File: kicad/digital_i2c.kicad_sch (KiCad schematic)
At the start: 21 parts, among them J10 Qwiic Cell Density, J11 Qwiic EZO-pH, J12 Qwiic EZO-ORP, J13 Qwiic EZO-DO, J14 Qwiic EZO-RTD, J15 Load Cell, J16 RS485 Hamilton, J8 Qwiic GPS SAM-M8Q, J9 Qwiic RTC DS3231, U14 HX711, U15 MAX485ESA, U21 ISO1541

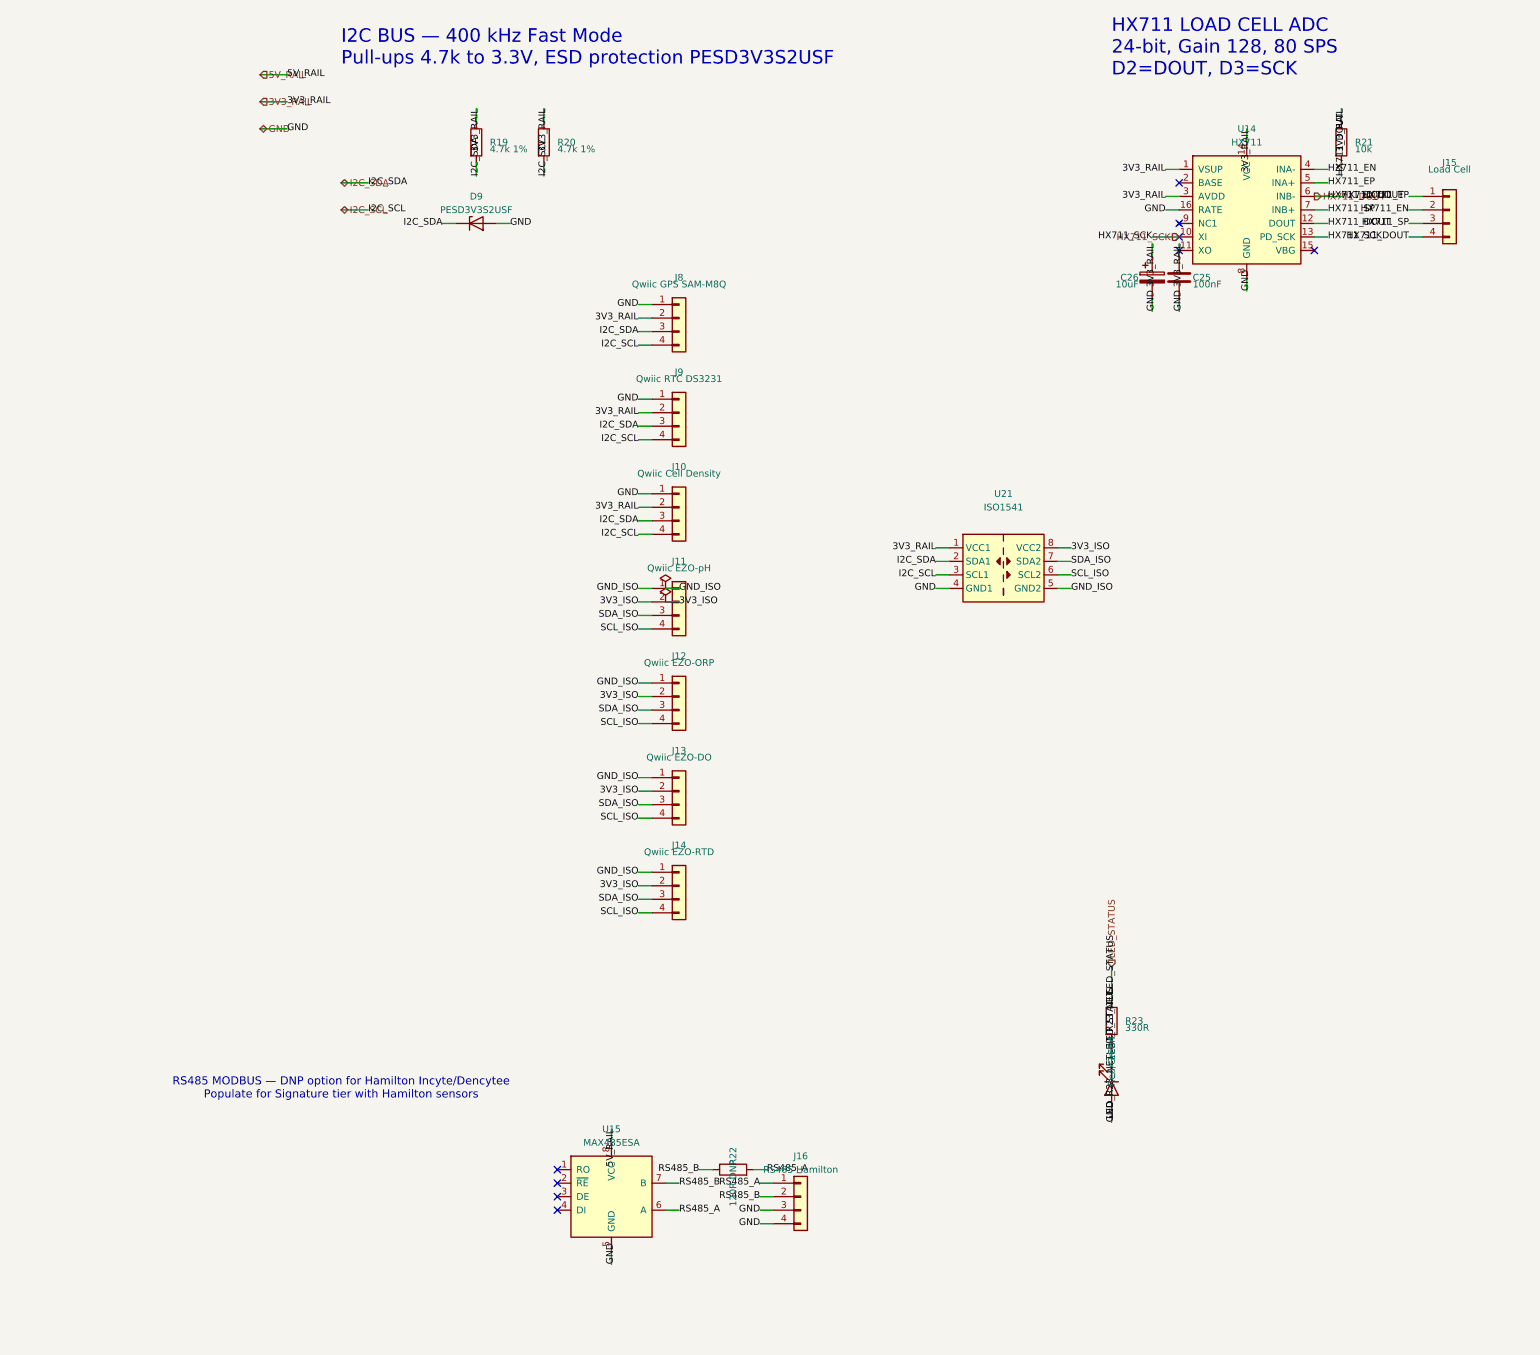
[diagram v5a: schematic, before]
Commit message: feat(rs485): SC16IS740 I2C-UART bridge + realign J21 pin map to firmware
RS485 Modbus had no digital interface: U15's RO/~RE/DE/DI were carrying
no-connect flags, so ERC stayed silent while the transceiver was unusable.
The UNO Q has no free UART TX/RX pair (USART1 is the HMI, the alternate
pairs land on analog pins), so Modbus now hangs off the I2C bus through an
SC16IS740 bridge and coexists with the HMI.

- U22 SC16IS740 on I2C at 0x4D (A0/A1 low), Y1 1.8432 MHz + C31/C32,
  C33 decoupling, R38 pull-up on the open-drain ~IRQ, exported to J21 D10
- U23 SN74LVC1G04 inverts ~RTS into DE/~RE. The bridge leaves ~RTS high
  after POR, which would enable the driver and seize the multidrop bus
  before firmware runs; inverted it resets to driver-off/receive-on
- U15 MAX485ESA -> MAX3485CSA+ (same SOIC-8 pinout) because the bridge is
  not 5 V tolerant; digital_i2c no longer needs the 5 V rail
- J21 realigned to the firmware: D4=MCU_WDI, D6=PUMP_DIR, D8=CHILLER_CTL,
  D9=CO2_PWM. WDI previously shared D8 with the chiller relay, so driving
  the chiller would have kicked the watchdog

ERC 0 under KiCad 10.0.5; netlist diff limited to the intended pins.

Co-Authored-By: Devin AI <158243242+devin-ai-integration[bot]@users.noreply.github.com>
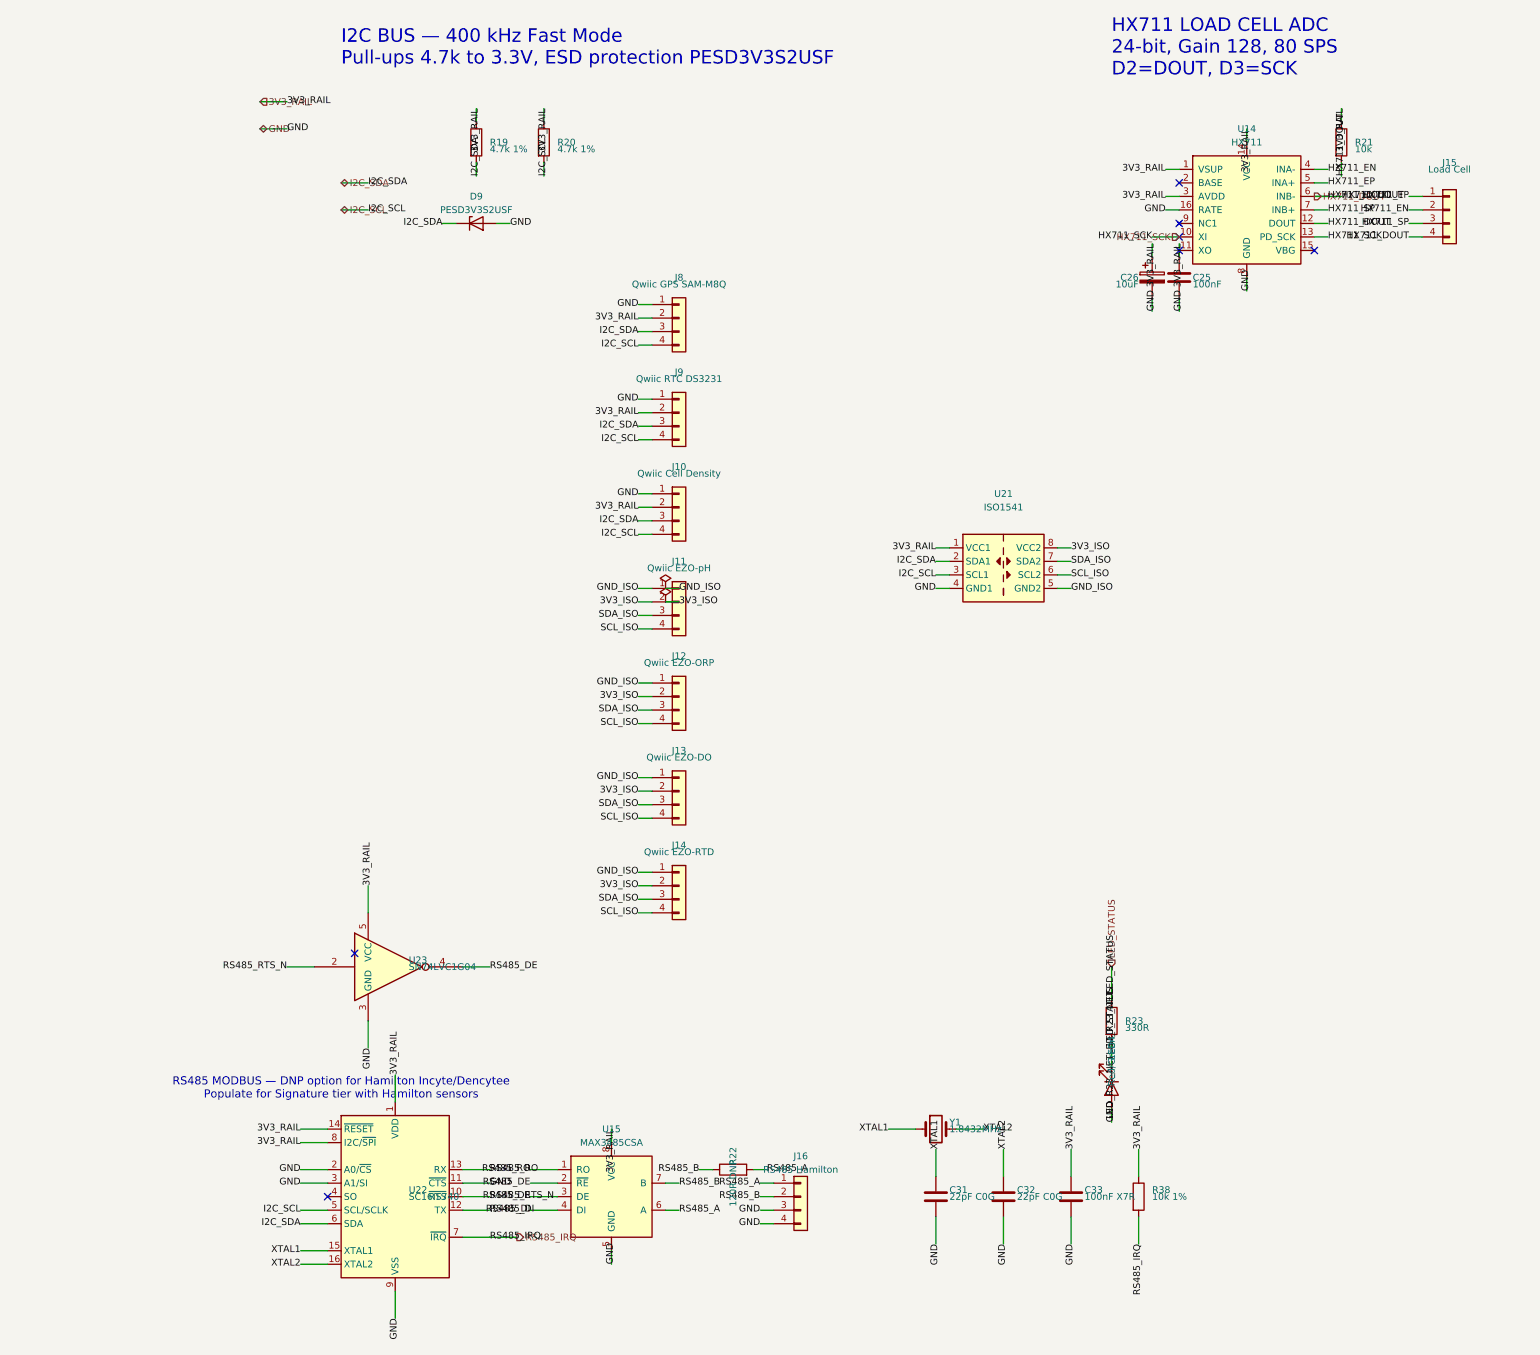
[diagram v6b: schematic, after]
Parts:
- added C31, C32: 22pF C0G, Capacitor_SMD:C_0402_1005Metric, symbol Device:C
- added C33: 100nF X7R, Capacitor_SMD:C_0402_1005Metric, symbol Device:C
- added R38: 10k 1%, Resistor_SMD:R_0402_1005Metric, symbol Device:R
- added U22: SC16IS740, Package_SO:TSSOP-16_4.4x5mm_P0.65mm, symbol Interface_UART:SC16IS740
- added U23: SN74LVC1G04, Package_TO_SOT_SMD:SOT-353_SC-70-5, symbol 74xGxx:74LVC1G04
- added Y1: 1.8432MHz, Crystal:Crystal_SMD_HC49-SD, symbol Device:Crystal
- U15: value MAX485ESA -> MAX3485CSA; symbol nebula_symbols:MAX485ESA -> nebula_symbols:MAX3485CSA
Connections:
- net 5V_RAIL is gone; now on net 3V3_RAIL: U15.8 (VCC)
- net 3V3_RAIL: now also C33.1, R38.1, U22.1 (VDD), U22.14 (~{RESET}), U22.8 (I2C/~{SPI}), U23.5 (VCC)
- net GND: now also C31.2, C32.2, C33.2, U22.11 (~{CTS}), U22.2 (A0/~{CS}), U22.3 (A1/SI), U22.9 (VSS), U23.3 (GND)
- net I2C_SCL: now also U22.5 (SCL/SCLK)
- net I2C_SDA: now also U22.6 (SDA)
- net RS485_RO: now reaches U15.1 (RO)
- net RS485_RO: now also U22.13 (RX)
- net RS485_DE: now reaches U15.2 (~{RE})
- net RS485_DE: now also U15.3 (DE), U23.4
- net RS485_DI: now reaches U15.4 (DI)
- net RS485_DI: now also U22.12 (TX)
- new net RS485_IRQ: R38.2, U22.7 (~{IRQ})
- new net RS485_RTS_N: U22.10 (~{RTS}), U23.2
- new net XTAL1: C31.1, U22.15 (XTAL1), Y1.1
- new net XTAL2: C32.1, U22.16 (XTAL2), Y1.2
- no-connect marks 9 -> 7
